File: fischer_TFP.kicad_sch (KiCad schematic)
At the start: 6 parts, among them J1 DIN41612_02x32_AC, J2 DIN41612_02x32_AC, J3 DIN41612_02x32_AC, J4 DIN41612_02x32_AC, J5 DIN41612_02x32_AC, J6 DIN41612_02x32_AC

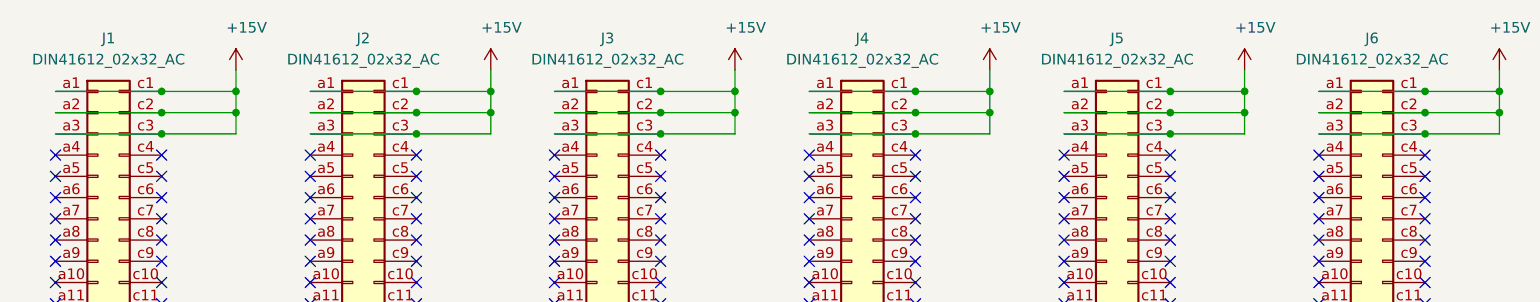
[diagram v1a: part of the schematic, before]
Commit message: Replaced constant current diode with KiCad device available as of v7.0.10 Updated LM5067 3D model
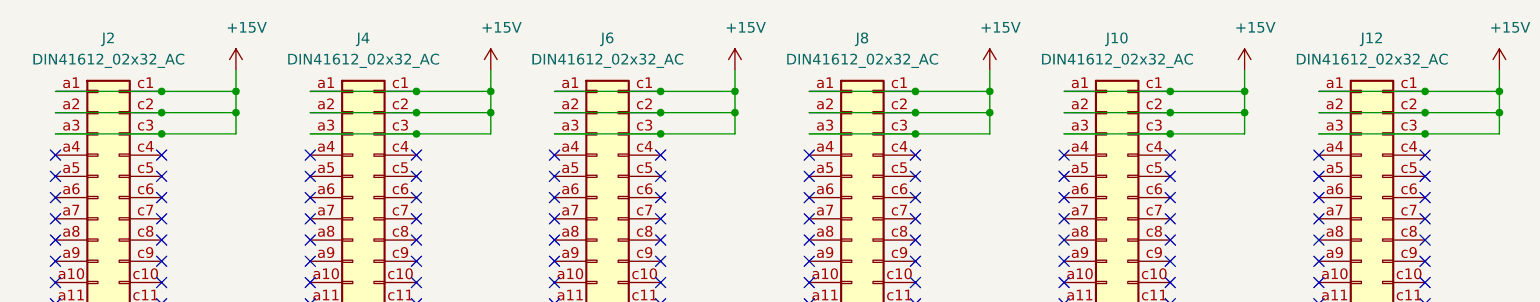
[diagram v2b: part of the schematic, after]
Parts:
- renumbered J5 to J10, J6 to J12, J1 to J2, J2 to J4, J3 to J6, J4 to J8
